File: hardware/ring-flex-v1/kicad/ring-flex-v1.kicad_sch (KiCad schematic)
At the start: 27 parts, among them J1 charge pad +, J2 charge pad -, M1 coin ERM 10x2.1mm, Q1A FS8205A (half), Q1B FS8205A (half), Q2 AO3400A, U1 MDBT50Q-1MV2, U2 MCP73831-2, U3 AP2112K-3.0 (3.0V, EN), U4 DW01A

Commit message: Hardware: footprints assigned, flex board outline
Decisions from the wearer: 10 mm band, magnetic charge contacts, closed ring,
65 mm circumference on the index finger, MCP73831 charger, keep the 1k gate
resistor, USB pads laid out but unpopulated, no LED, no button, JLCPCB, port
the bootloader variant.

Footprints assigned to every part except the three that need real land
patterns: U1 (MDBT50Q module), M1 (motor) and BT1 (cell). Those stay empty
rather than invented -- a fabricated land pattern passes every check and
arrives as a dead board.

New ring-flex-v1.kicad_pcb carries the 65.0 x 10.0 mm outline on Edge.Cuts
with the island and bend zones marked on Dwgs.User, the antenna keep-out on
User.1, and the layout rules as board text. DRC: 0 violations.

Motor rail set to 3.0 V. Rail voltage does not change motor thickness, only
output; 3.3 V is a one-resistor change if the 2.1 mm motor feels weak.

Co-Authored-By: Claude Opus 5 <noreply@anthropic.com>
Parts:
- C1: footprint (none) -> Capacitor_SMD:C_1206_3216Metric
- C2: footprint (none) -> Capacitor_SMD:C_0805_2012Metric
- C3: footprint (none) -> Capacitor_SMD:C_0603_1608Metric
- C4, C5, C6: footprint (none) -> Capacitor_SMD:C_0402_1005Metric
- D1, D2: footprint (none) -> Diode_SMD:D_SOD-323
- J1, J2, TP1, TP2, TP3, TP4: footprint (none) -> TestPoint:TestPoint_Pad_D1.0mm
- Q1A, Q1B, U4: footprint (none) -> Package_TO_SOT_SMD:SOT-23-6
- Q2: footprint (none) -> Package_TO_SOT_SMD:SOT-23
- R1, R2, R3, R4: footprint (none) -> Resistor_SMD:R_0402_1005Metric
- U2, U3: footprint (none) -> Package_TO_SOT_SMD:SOT-23-5

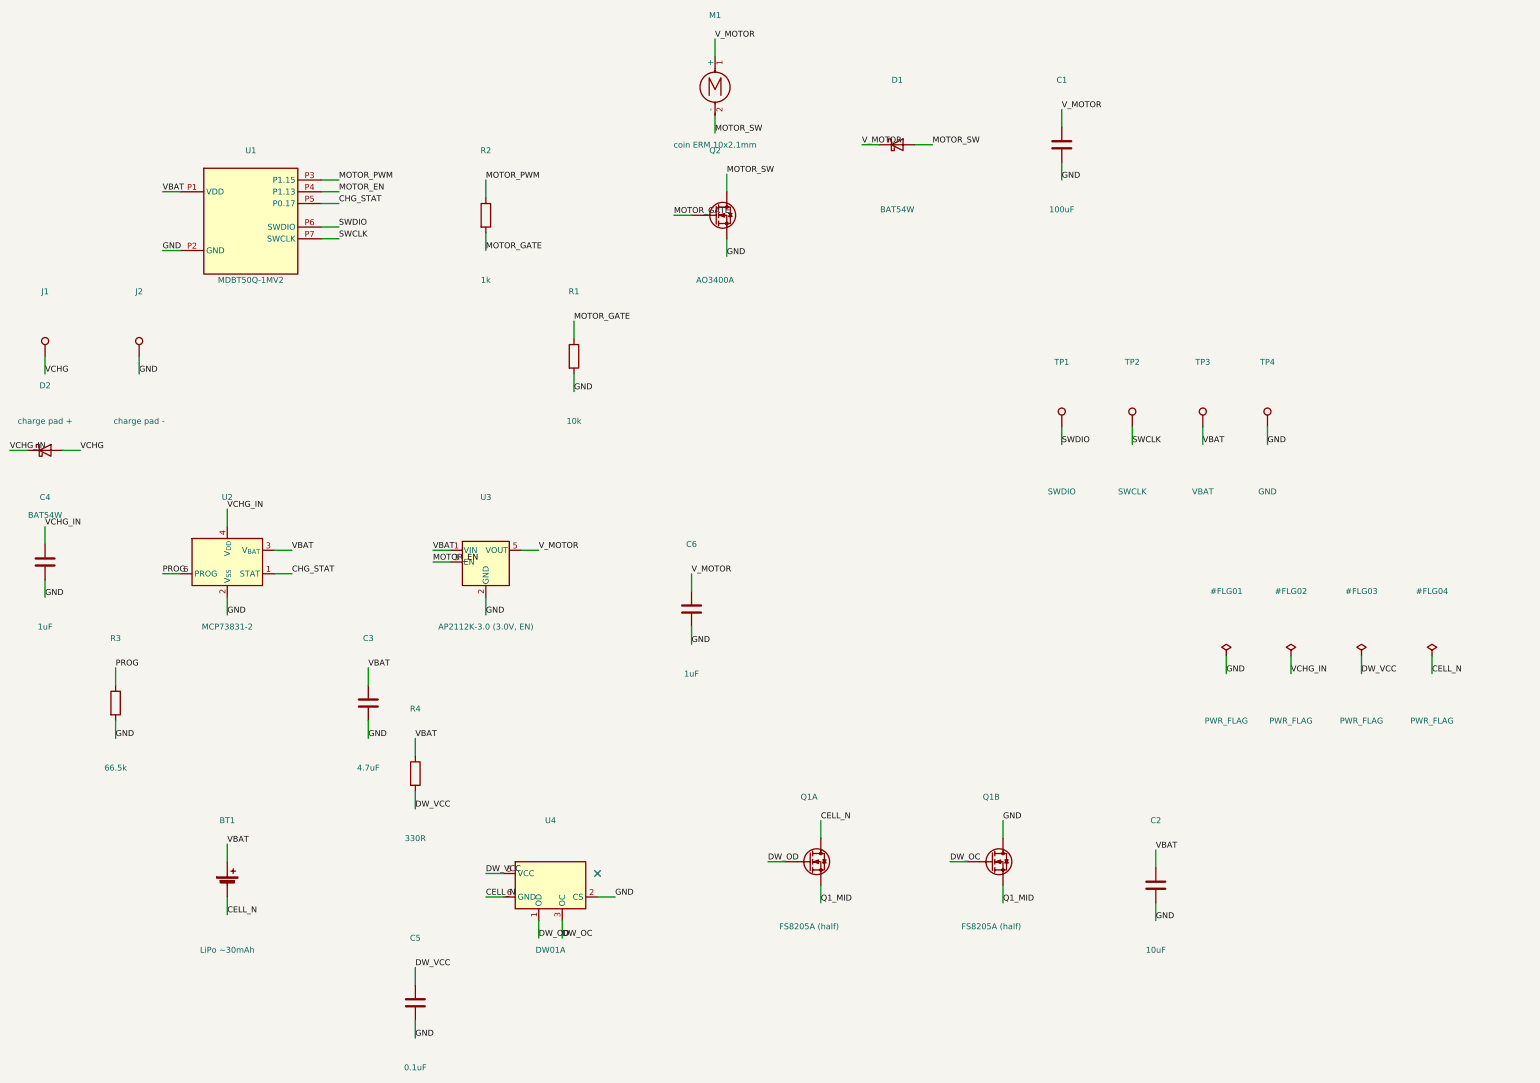
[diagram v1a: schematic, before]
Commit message: Hardware: motor and cell footprints; real motor part identified
Two of the three missing footprints are done. Both are wire-attach pads,
which is a choice I am making rather than a vendor land pattern I would be
inventing - these motors and cells ship with flying leads, so there is no
land pattern to get wrong. Each footprint says so in its description.

  Motor_Coin_10mm_WirePads     10 mm body outline, 2 pads for AWG32 leads
  Battery_LiPo_16x8_WirePads   16 x 8 mm keep-out, 2 pads

Both render through kicad-cli. U1 remains without a footprint: the module's
61-pad land pattern has to come from Raytac.

Motor part identified and corrected. The "10 x 2.1 mm, 1.1 G at 233 Hz"
figure I quoted earlier came from a comparison table with no part number
behind it, not from a real product -- Precision Microdrives' actual 10 mm
coin is the 310-101 at 3.4 mm, which is what is already on the ring. The
purchasable thin part is the NFP-C1020: 10.0 x 2.0 mm, 3.0 V, 80 mA max,
11,000 rpm.

Two cautions now recorded in the BOM:

- The vendor's own page gives two different amplitudes for this motor, 0.80G
  in the prose and 1.10G in the spec table, and does the same thing on the
  C1030 elsewhere. Their figures cannot be trusted; the decision still rests
  on comparing it by hand against the motor already in service.
- 11,000 rpm is about 183 Hz, the same as the current motor. There is no
  frequency advantage here, only less output for 1.4 mm less thickness.

Also: the 2.0 mm thickness excludes the adhesive foam, and the cell at
2.5 mm is now the thickest part on the board.

Co-Authored-By: Claude Opus 5 <noreply@anthropic.com>
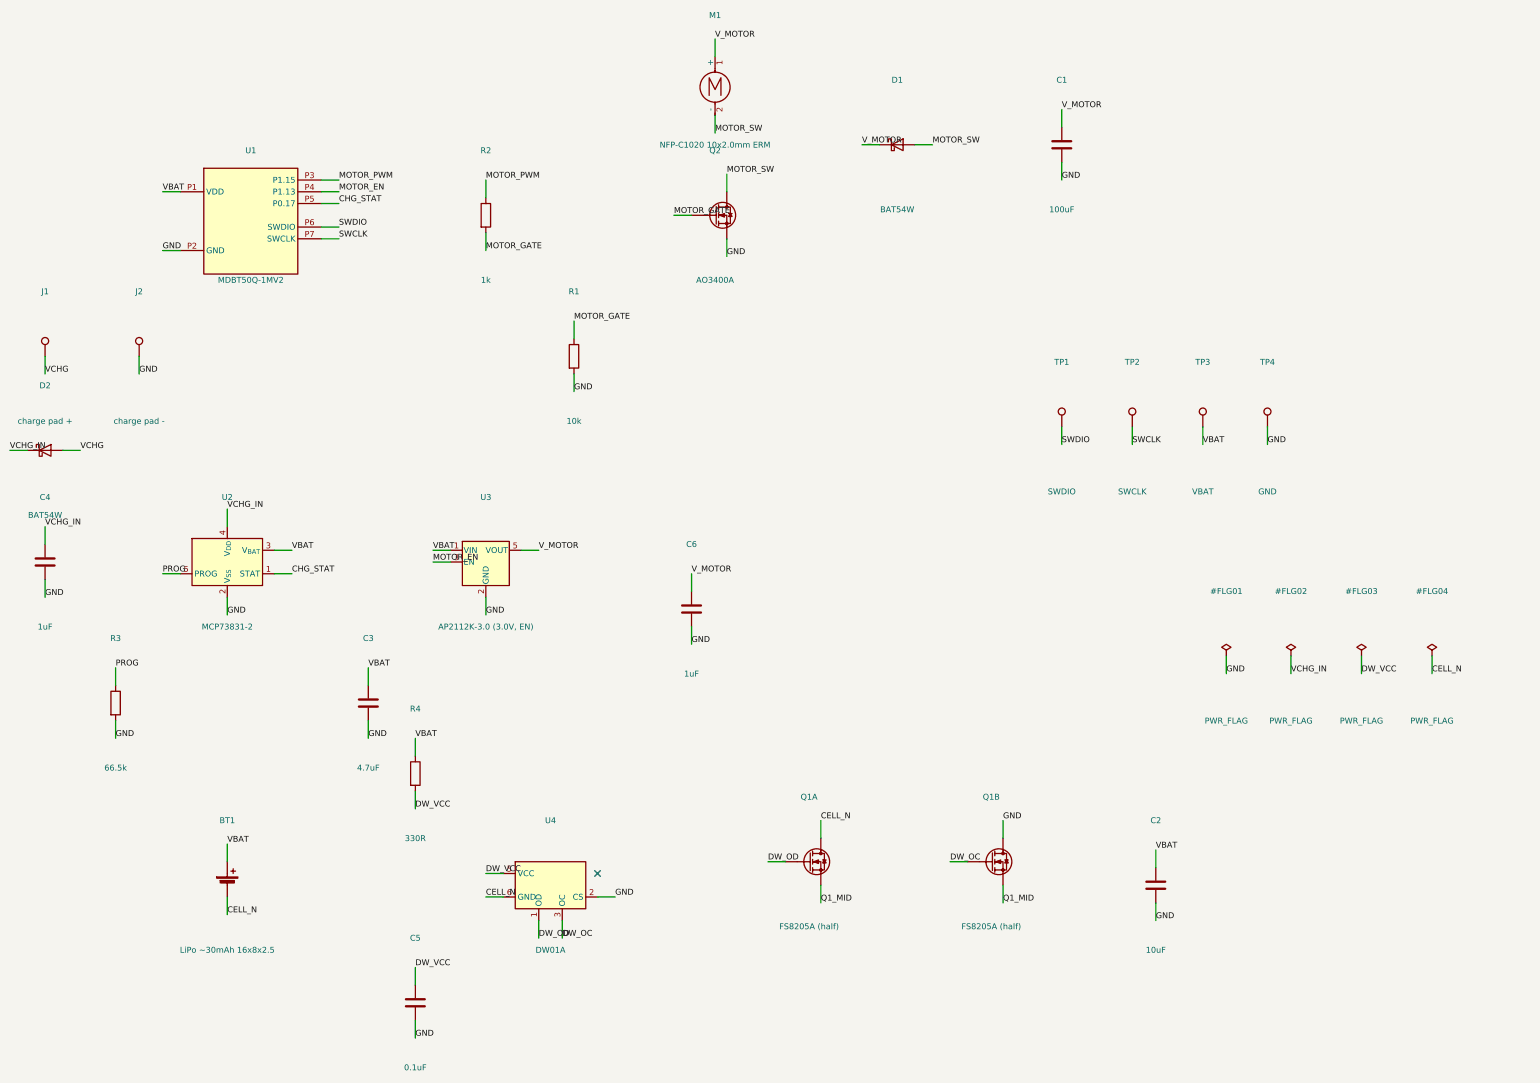
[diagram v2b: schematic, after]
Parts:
- BT1: value LiPo ~30mAh -> LiPo ~30mAh 16x8x2.5; footprint (none) -> ring-flex-v1:Battery_LiPo_16x8_WirePads
- M1: value coin ERM 10x2.1mm -> NFP-C1020 10x2.0mm ERM; footprint (none) -> ring-flex-v1:Motor_Coin_10mm_WirePads

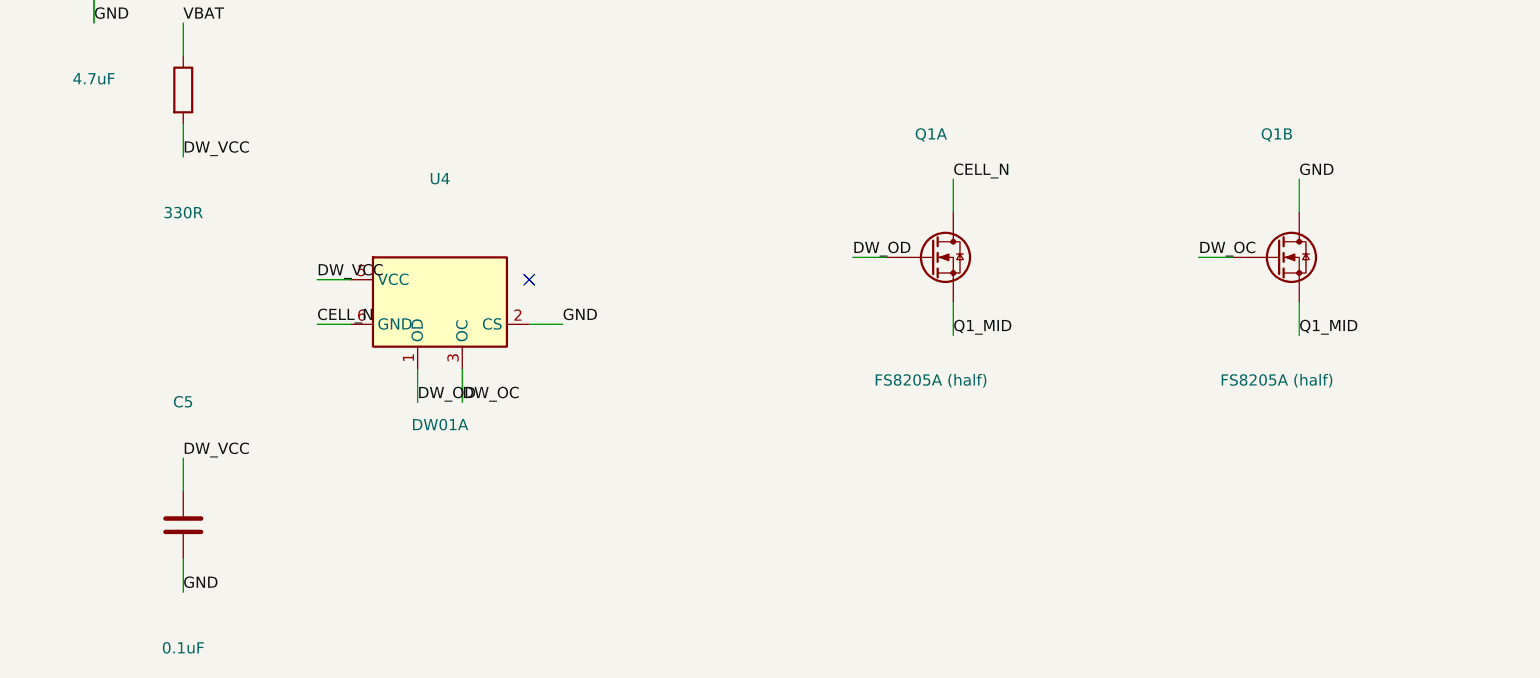
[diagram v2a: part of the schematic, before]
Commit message: Hardware: fix the cell protection circuit against the datasheets
Three errors, all in the part I built from memory rather than from a
reference. Found by reading the FS8205A and DW01A datasheets.

1. THE FETS WERE WIRED BACKWARDS. I had the FS8205A's two MOSFETs tied
   source-to-source. The datasheet's own marking diagram is

       G1    D1/D2    G2
              8205A
       S1    D1/D2    S2

   so the part shares its DRAINS. Q1_MID is now the common drain, S1 goes to
   the cell negative and S2 to pack negative. As drawn before, the
   protection would not have worked.

2. R4 was 330 R. The DW01A datasheet sets a 470 R minimum for R1. Now 1 k.

3. R5 was missing entirely. CS was tied straight to pack negative; the
   datasheet states plainly that R1 and R2 cannot be omitted. Added 2 k,
   mid-range of the specified 1-3 k.

Verified in the exported netlist: CELL_N carries BT1.2, Q1A.S and U4.6;
Q1_MID carries Q1A.D and Q1B.D; GND carries Q1B.S; DW_CS carries R5.1 and
U4.2.

ERC is down to a single warning, lib_symbol_mismatch on the AP2112K. That is
expected: the symbol is a derived one, so the embedded copy holds the
resolved parent body rather than the library's "extends" form.

Co-Authored-By: Claude Opus 5 <noreply@anthropic.com>
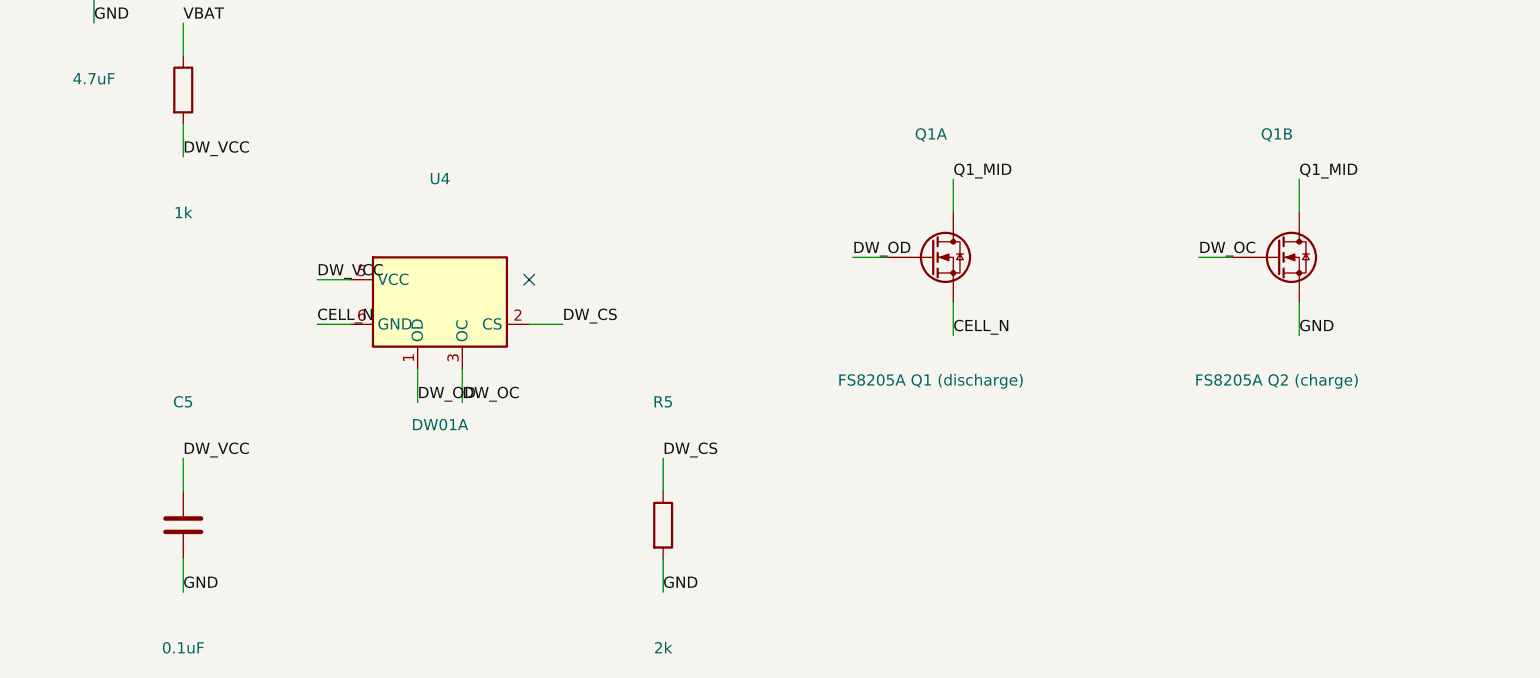
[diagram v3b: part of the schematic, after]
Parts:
- added R5: 2k, Resistor_SMD:R_0402_1005Metric, symbol Device:R
- Q1A: value FS8205A (half) -> FS8205A Q1 (discharge)
- Q1B: value FS8205A (half) -> FS8205A Q2 (charge)
- R4: value 330R -> 1k
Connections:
- net CELL_N: now also Q1A.S; no longer Q1A.D
- net GND: now also Q1B.S, R5.2; no longer Q1B.D, U4.2 (CS)
- net Q1_MID: now also Q1A.D, Q1B.D; no longer Q1A.S, Q1B.S
- new net DW_CS: R5.1, U4.2 (CS)

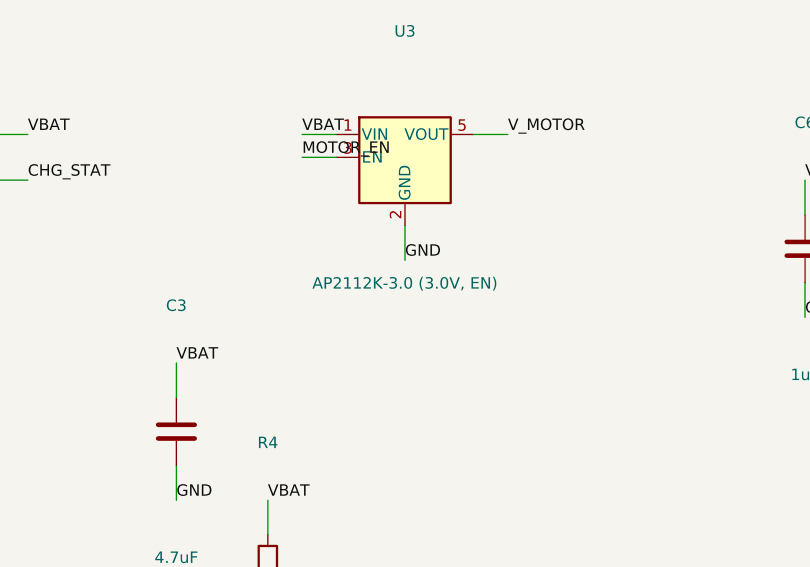
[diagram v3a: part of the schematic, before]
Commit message: Hardware: real LDO part, and the charger's tolerance band
U3 was a placeholder. It is now TPS7A0230PDBVR: 3.0 V fixed, SOT-23-5,
200 mA, 25 nA quiescent.

Two properties of that part matter to this design:

- Its EN pin has an internal pulldown, so the motor rail is off at power-on
  and stays off until firmware drives EN high. That is the same fail-safe
  R1 gives the motor gate, and it means a reset or a spell in the bootloader
  cannot leave the rail live.
- Dropout is 270 mV max at 200 mA, and the motor draws about 85 mA, so the
  3.0 V rail still regulates well below the 3300 mV cutoff. That answers the
  worry from the POC, where the cutoff sat awkwardly close to the XIAO
  regulator's dropout.

MCP73831 verified against the datasheet rather than memory: programmable
15-500 mA, R_PROG 2-67 kOhm, I = 1000/R with R in kOhm. R3 at 66.5 k gives
15 mA typical, but the band at 67 k is 12.5 / 15 / 16.5 mA -- so the cell has
to tolerate 16.5 mA, which on 30 mAh is 0.55C rather than the 0.5C I quoted.
Anything above 67 k falls into the shutdown zone, so 66.5 k sits on the right
side of that edge. R3 is specified 1%.

ERC unchanged at one cosmetic lib_symbol_mismatch.

Co-Authored-By: Claude Opus 5 <noreply@anthropic.com>
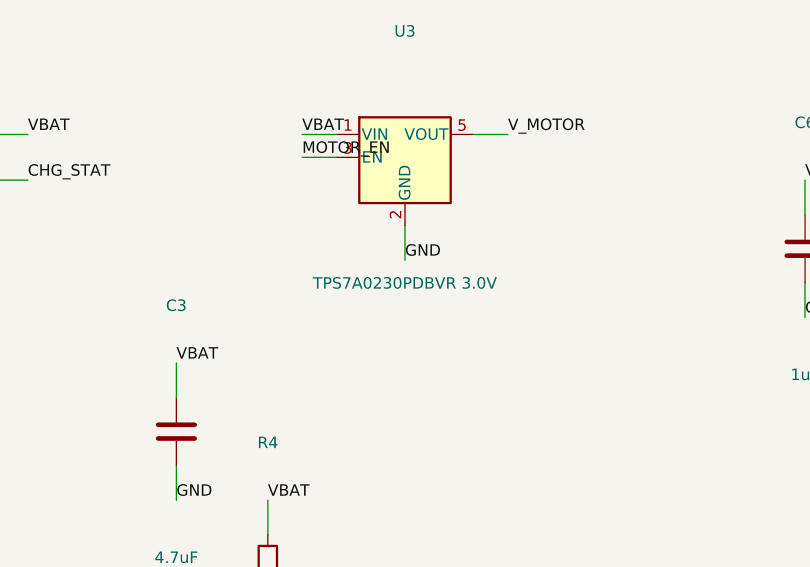
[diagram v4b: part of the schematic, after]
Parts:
- U3: value AP2112K-3.0 (3.0V, EN) -> TPS7A0230PDBVR 3.0V
